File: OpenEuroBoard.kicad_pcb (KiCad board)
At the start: 2 copper layers, 300 x 100 mm, 143 parts, among them J1 Eurorack_bus_mini, J10 Jack 4, J11 Conn_01x08, J12 Jack 5, J13 Jack 6, J14 Jack 7, J15 Jack 8, J16 Conn_01x04, J17 MIDI_in, J18 Conn_01x03, J19 Conn_01x03, J2 Conn_01x07, J20 Conn_01x03, J21 MIDI_out, J22 Conn_01x03, J23 Conn_01x05, J24 Conn_01x03, J25 Conn_01x05, J26 Conn_01x03, J27 Conn_01x08, J28 Conn_01x08, J29 Conn_01x04, J3 Conn_01x07, J30 Screw_Terminal_01x01, J31 Conn_01x05, J32 Conn_01x03, J33 Conn_01x05, J34 Conn_01x03, J35 Conn_01x05, J36 Conn_01x03, J37 Screw_Terminal_01x01, J38 Screw_Terminal_01x01, J39 Conn_01x05, J4 Conn_01x07, J40 Conn_01x03, J41 Conn_01x03, J42 Conn_01x05, J43 Conn_01x03, J44 Conn_01x03, J45 Conn_01x02, J46 Conn_01x04, J47 Screw_Terminal_01x01, J48 Screw_Terminal_01x01, J49 Screw_Terminal_01x01, J5 Conn_01x07, J50 Screw_Terminal_01x01, J51 Screw_Terminal_01x01, J52 Conn_01x04, J53 Conn_01x04, J54 Conn_01x04, J55 Jumpers, J56 Conn_01x04, J57 Conn_01x08, J58 Conn_01x02, J59 AudioJack3_Ground, J6 Jack 1, J7 Jack 2, J8 Conn_01x08, J9 Jack 3, SW1 SW_Push, SW10 SW_SPDT, SW11 SW_SPDT, SW12 SW_SPDT, SW2 SW_Push, SW3 SW_Push, SW4 SW_Push, SW5 SW_Push, SW6 SW_Push, SW7 SW_SPDT, SW8 SW_SPDT, SW9 SW_SPDT, U1 LM1117IMP-5, U2 TL074, U3 TL074, U4 CD40107BE, U5 6N139, U6 TL074, U7 TL072, U8 TL074

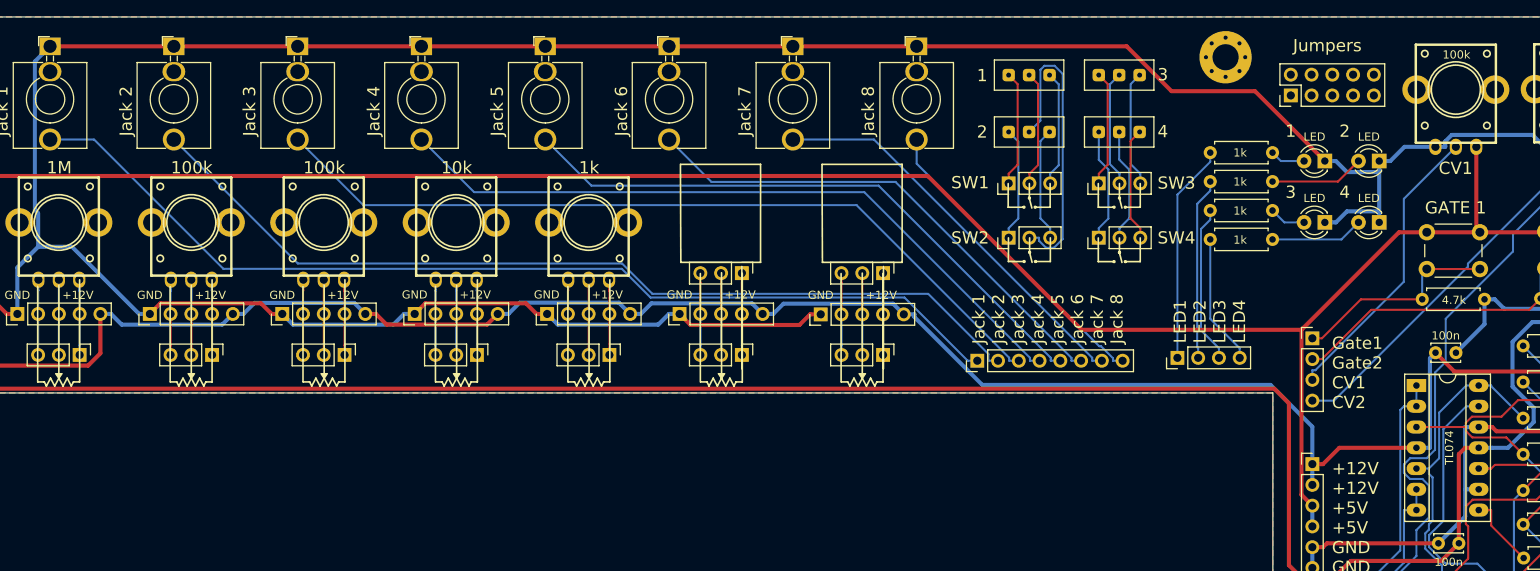
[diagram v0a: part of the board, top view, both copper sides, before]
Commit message: Add connector for normals to jacks
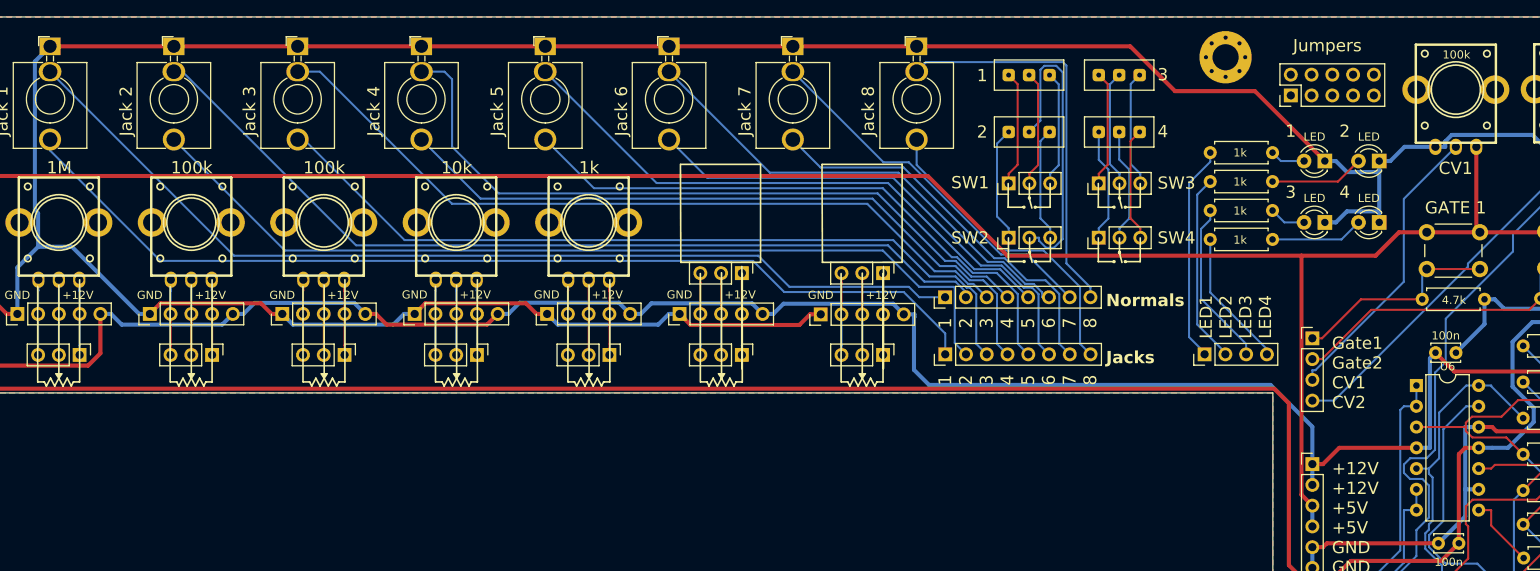
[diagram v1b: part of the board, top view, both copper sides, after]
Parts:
- added J60: Conn_01x08, Connector_PinHeader_2.54mm:PinHeader_1x08_P2.54mm_Vertical, F.Cu at (192.4, 34.3)
- U6: footprint Package_DIP:DIP-14_W7.62mm_Socket_LongPads -> Package_DIP:DIP-14_W7.62mm
- moved J11 4.00 mm to (192.4, 41.3)
- moved J16 3.36 mm to (224.2, 41.3)
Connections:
- J10 pad TN: unconnected-(J10-PadTN) -> Net-(J60-Pin_4)
- J12 pad TN: unconnected-(J12-PadTN) -> Net-(J60-Pin_5)
- J13 pad TN: unconnected-(J13-PadTN) -> Net-(J60-Pin_6)
- J14 pad TN: unconnected-(J14-PadTN) -> Net-(J60-Pin_7)
- J15 pad TN: unconnected-(J15-PadTN) -> Net-(J60-Pin_8)
- J6 pad TN: unconnected-(J6-PadTN) -> Net-(J60-Pin_1)
- J7 pad TN: unconnected-(J7-PadTN) -> Net-(J60-Pin_2)
- J9 pad TN: unconnected-(J9-PadTN) -> Net-(J60-Pin_3)
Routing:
- net Net-(J60-Pin_1): track 0.00 -> 120.9 mm
- net Net-(J60-Pin_2): track 0.00 -> 108.7 mm
- net Net-(J60-Pin_3): track 0.00 -> 95.7 mm
- net Net-(J60-Pin_4): track 0.00 -> 88.0 mm
- net Net-(J60-Pin_5): track 0.00 -> 70.5 mm
- net Net-(J60-Pin_6): track 0.00 -> 58.3 mm
- net Net-(J60-Pin_8): track 0.00 -> 48.5 mm
- net Net-(J60-Pin_7): track 0.00 -> 45.3 mm
- net +12V: track 512.6 -> 516.4 mm
- net Net-(J11-Pin_1): track 124.7 -> 122.7 mm
- net +5V: track 440.0 -> 441.5 mm
- net Net-(J16-Pin_4): track 16.0 -> 16.9 mm
- net Net-(J16-Pin_3): track 19.4 -> 20.4 mm
- net Net-(J16-Pin_2): track 22.3 -> 23.2 mm
- net Net-(J11-Pin_3): track 99.7 -> 98.8 mm
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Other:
- board text added: "1 2 3 4 5 6 7 8"
- board text added: "Jacks"
- board text added: "Normals"
- board text removed: "Jack 1 Jack 2 Jack 3 Jack 4 Jack 5 Jack 6 Jack 7 Jack 8"
